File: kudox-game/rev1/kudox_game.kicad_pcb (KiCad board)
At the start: 2 copper layers, 145.7 x 130.4 mm, 65 parts, among them K0 KEYSW, K1 KEYSW, K11 KEYSW, K12 KEYSW, K13 KEYSW, K14 KEYSW, K15 KEYSW, K2 KEYSW, K20 KEYSW, K21 KEYSW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

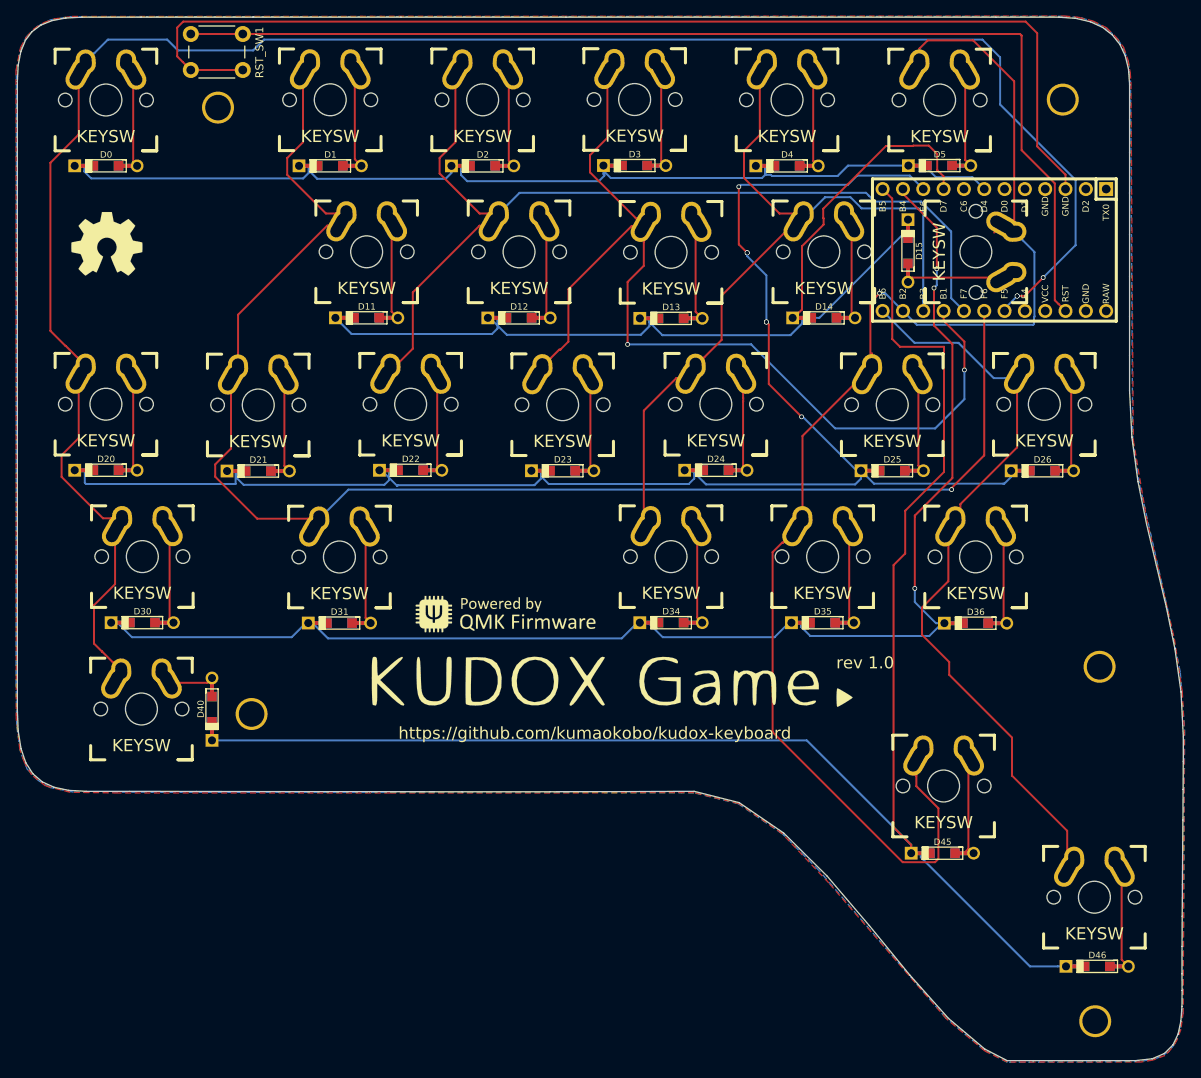
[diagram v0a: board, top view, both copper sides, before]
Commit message: [kudox-game] Modified alignments of some switches. (#33)
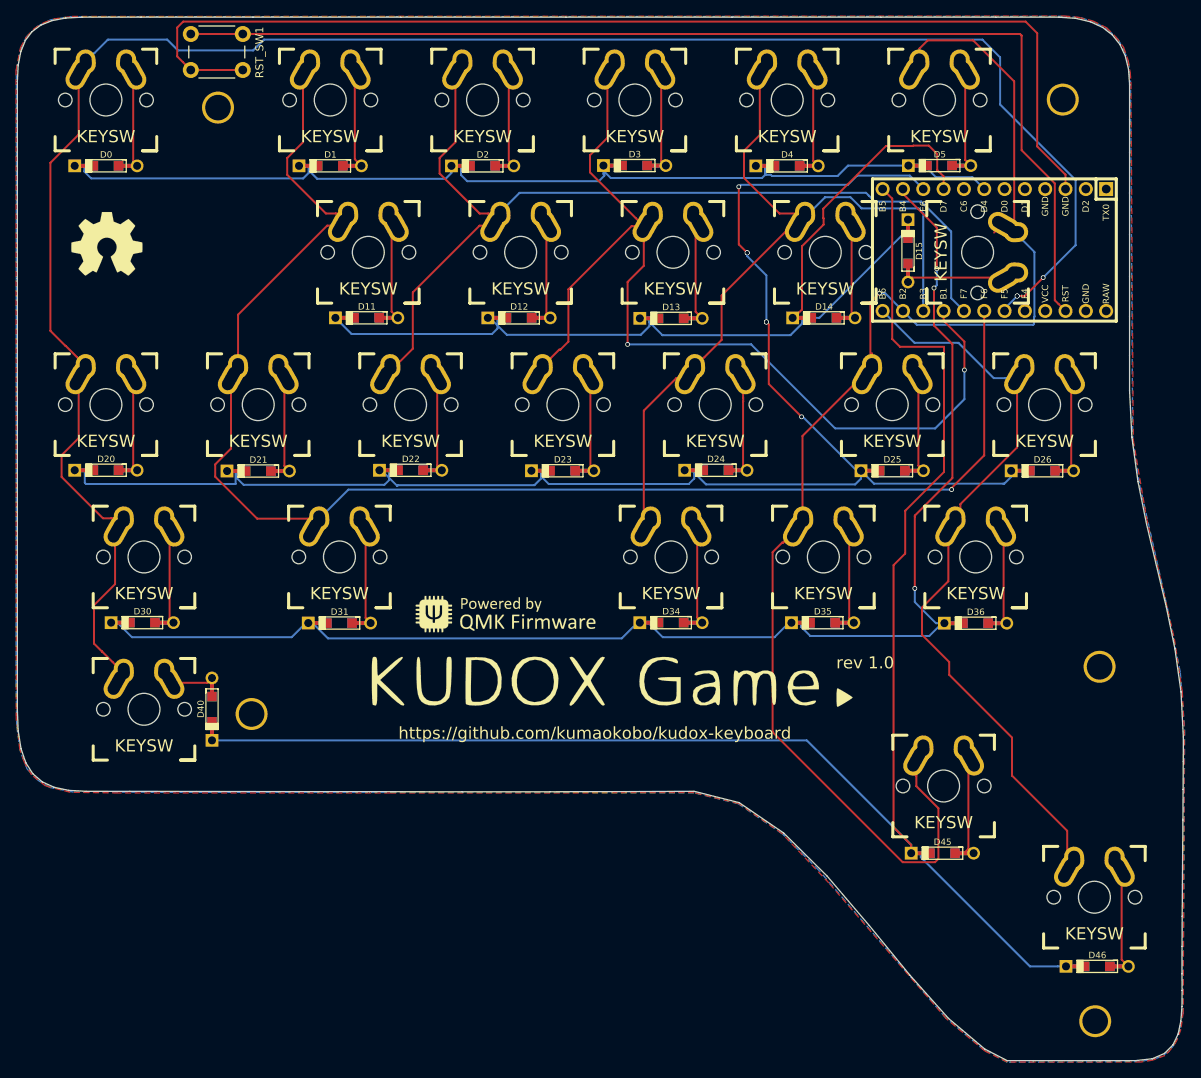
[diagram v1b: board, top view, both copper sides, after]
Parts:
- G*** (x2): footprint myparts:qmk-badge -> kudox_game_footprints:qmk-badge
- K0, K20: footprint myparts:Mx_Alps_125-dualside -> kudox_game_footprints:Mx_Alps_100-dualside
- K30: footprint myparts:Mx_Alps_125-dualside -> kudox_game_footprints:Mx_Alps_125-dualside
- moved K40 0.32 mm to (95.5, 136.5)
- moved K13 0.24 mm to (161.6, 79.4)
- moved K15 0.23 mm to (199.7, 79.4)
- moved K11 0.22 mm to (123.5, 79.4)
- moved K30 0.21 mm to (95.5, 117.5)
- moved K12 0.21 mm to (142.5, 79.4)
- moved K14 0.19 mm to (180.6, 79.4)
- moved K35 0.10 mm to (180.4, 117.5)
- moved K24 0.09 mm to (166.8, 98.4)
- moved K3 0.07 mm to (156.8, 60.4)
- moved K20 0.06 mm to (90.7, 98.4)
- moved K26 0.05 mm to (208.0, 98.4)
- moved K22 0.05 mm to (128.8, 98.4)
